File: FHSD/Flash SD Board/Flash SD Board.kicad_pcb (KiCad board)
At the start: 2 copper layers, 27.9 x 25.8 mm, 5 parts, among them J501 Conn_01x07_Male, U10 W25N512GVPIT

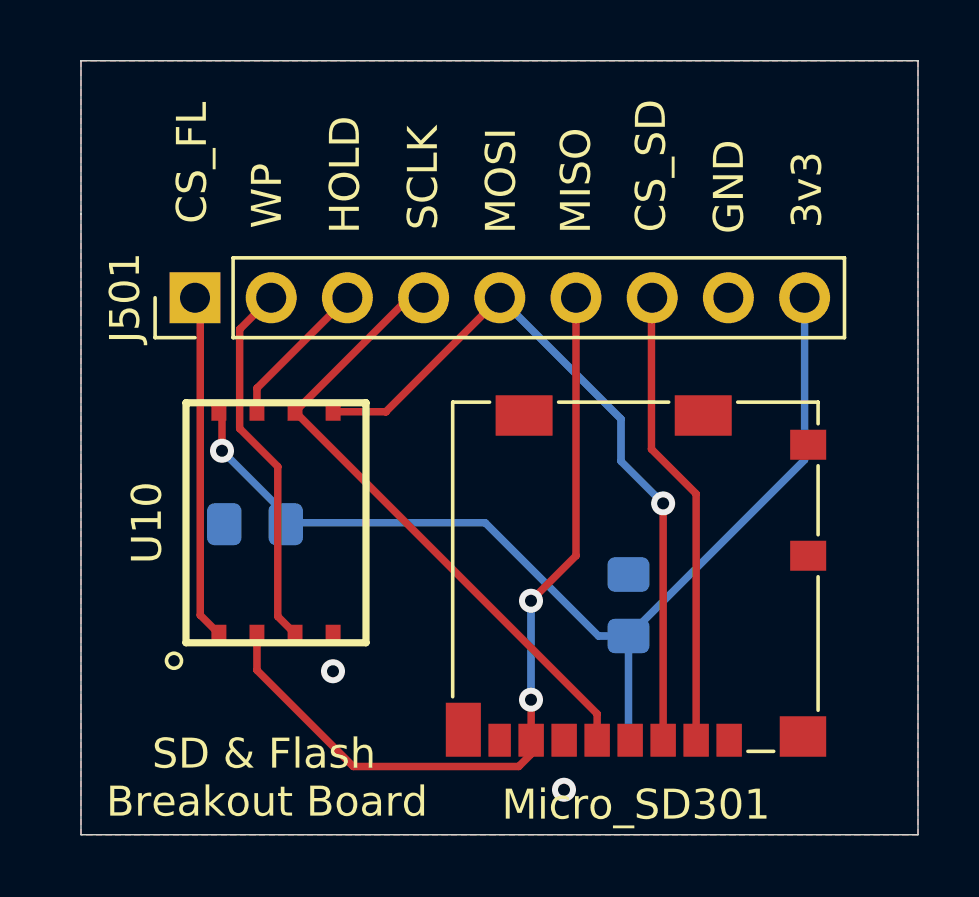
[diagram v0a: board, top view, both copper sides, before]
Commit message: Matthew you forgot to connect a pin :(
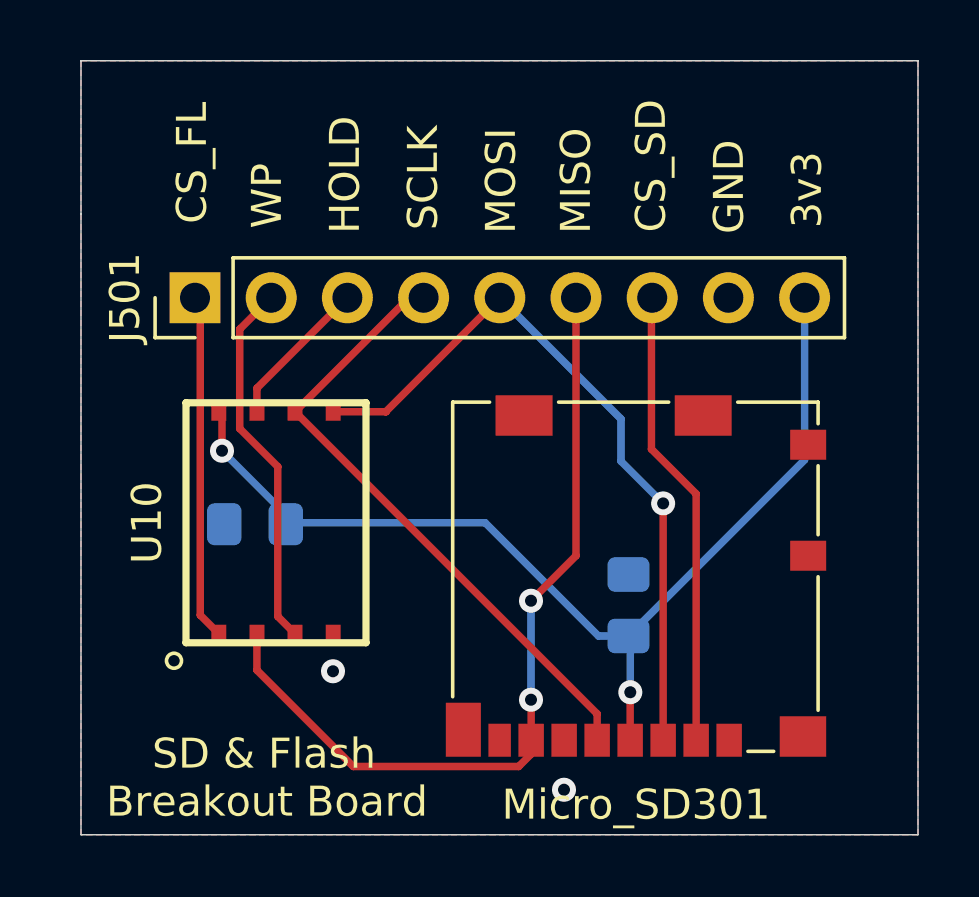
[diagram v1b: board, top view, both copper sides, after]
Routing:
- net +3V3: track 35.3 -> 35.4 mm, vias 1 -> 2
